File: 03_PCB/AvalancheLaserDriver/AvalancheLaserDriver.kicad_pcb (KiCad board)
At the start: 2 copper layers, 57 x 32 mm, 58 parts, among them IC1 LT8365JMSE, J1 694106106102, J2 SMA, J3 Conn_01x02_Pin, J4 SMA, Q1 PJA3463_R1_00001, Q2 FMMT417TD, SW1 JS202011JAQN

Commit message: feat(pcb): edit component values after assembling first prototype
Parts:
- C9: value 100n;500V -> 22n;500V
- D8: value SD103AWS -> SD103AWS/PMEG3005EJ
- R1: value 100k -> 100k;1%
- R2: value 47k -> 47k;1%
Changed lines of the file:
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@@
 			)
 		)
-		(property "Value" "SD103AWS"
+		(property "Value" "SD103AWS/PMEG3005EJ"
 			(at 0.1 1.9 0)
 			(layer "F.Fab")
@@
 		(property ki_fp_filters "BarrelJack*")
 		(sheetname "/")
-		(sheetfile "LightspeedLaserDriver.kicad_sch")
+		(sheetfile "AvalancheLaserDriver.kicad_sch")
 		(attr smd)
 		(fp_circle
@@
 		(property ki_fp_filters "MountingHole*")
 		(sheetname "/")
-		(sheetfile "LightspeedLaserDriver.kicad_sch")
+		(sheetfile "AvalancheLaserDriver.kicad_sch")
 		(attr exclude_from_pos_files exclude_from_bom)
 		(fp_circle
@@
 		(property ki_fp_filters "LED* LED_SMD:* LED_THT:*")
 		(sheetname "/")
-		(sheetfile "LightspeedLaserDriver.kicad_sch")
+		(sheetfile "AvalancheLaserDriver.kicad_sch")
 		(attr smd)
 		(fp_line
@@
 			)
 		)
-		(property "Value" "100k"
+		(property "Value" "100k;1%"
 			(at 0 1.43 0)
 			(layer "F.Fab")
@@
 		(property ki_fp_filters "R_*")
 		(sheetname "/")
-		(sheetfile "LightspeedLaserDriver.kicad_sch")
+		(sheetfile "AvalancheLaserDriver.kicad_sch")
 		(attr smd)
 		(fp_line
@@
 		(property ki_fp_filters "Connector*:*_1x??_*")
 		(sheetname "/")
-		(sheetfile "LightspeedLaserDriver.kicad_sch")
+		(sheetfile "AvalancheLaserDriver.kicad_sch")
 		(attr smd)
 		(fp_rect
@@
 		(property ki_fp_filters "TO-???* *_Diode_* *SingleDiode* D_*")
 		(sheetname "/")
-		(sheetfile "LightspeedLaserDriver.kicad_sch")
+		(sheetfile "AvalancheLaserDriver.kicad_sch")
 		(attr smd)
 		(fp_line
@@
 		(property ki_fp_filters "MountingHole*")
 		(sheetname "/")
-		(sheetfile "LightspeedLaserDriver.kicad_sch")
+		(sheetfile "AvalancheLaserDriver.kicad_sch")
 		(attr exclude_from_pos_files exclude_from_bom)
 		(fp_circle
@@
 		(property ki_fp_filters "*Fuse*")
 		(sheetname "/")
-		(sheetfile "LightspeedLaserDriver.kicad_sch")
+		(sheetfile "AvalancheLaserDriver.kicad_sch")
 		(attr smd)
 		(fp_line
@@
 		(property ki_fp_filters "MountingHole*")
 		(sheetname "/")
-		(sheetfile "LightspeedLaserDriver.kicad_sch")
+		(sheetfile "AvalancheLaserDriver.kicad_sch")
 		(attr exclude_from_pos_files exclude_from_bom)
 		(fp_circle
@@
 			)
 		)
-		(property "Value" "100n;500V"
+		(property "Value" "22n;500V"
 			(at 0 1.68 90)
 			(layer "F.Fab")
@@
 		(property ki_fp_filters "MountingHole*")
 		(sheetname "/")
-		(sheetfile "LightspeedLaserDriver.kicad_sch")
+		(sheetfile "AvalancheLaserDriver.kicad_sch")
 		(attr exclude_from_pos_files exclude_from_bom)
 		(fp_circle
@@
 		)
 		(sheetname "/")
-		(sheetfile "LightspeedLaserDriver.kicad_sch")
+		(sheetfile "AvalancheLaserDriver.kicad_sch")
 		(attr smd)
 		(fp_line
@@
 			)
 		)
-		(property "Value" "47k"
+		(property "Value" "47k;1%"
 			(at 0 1.43 0)
 			(layer "F.Fab")
@@
 		(property ki_fp_filters "R_*")
 		(sheetname "/")
-		(sheetfile "LightspeedLaserDriver.kicad_sch")
+		(sheetfile "AvalancheLaserDriver.kicad_sch")
 		(attr smd)
 		(fp_line
@@
 		(property ki_fp_filters "*BNC* *SMA* *SMB* *SMC* *Cinch* *LEMO* *UMRF* *MCX* *U.FL*")
 		(sheetname "/")
-		(sheetfile "LightspeedLaserDriver.kicad_sch")
+		(sheetfile "AvalancheLaserDriver.kicad_sch")
 		(attr through_hole)
 		(fp_line
@@
 		(property ki_fp_filters "*BNC* *SMA* *SMB* *SMC* *Cinch* *LEMO* *UMRF* *MCX* *U.FL*")
 		(sheetname "/")
-		(sheetfile "LightspeedLaserDriver.kicad_sch")
+		(sheetfile "AvalancheLaserDriver.kicad_sch")
 		(attr through_hole)
 		(fp_line

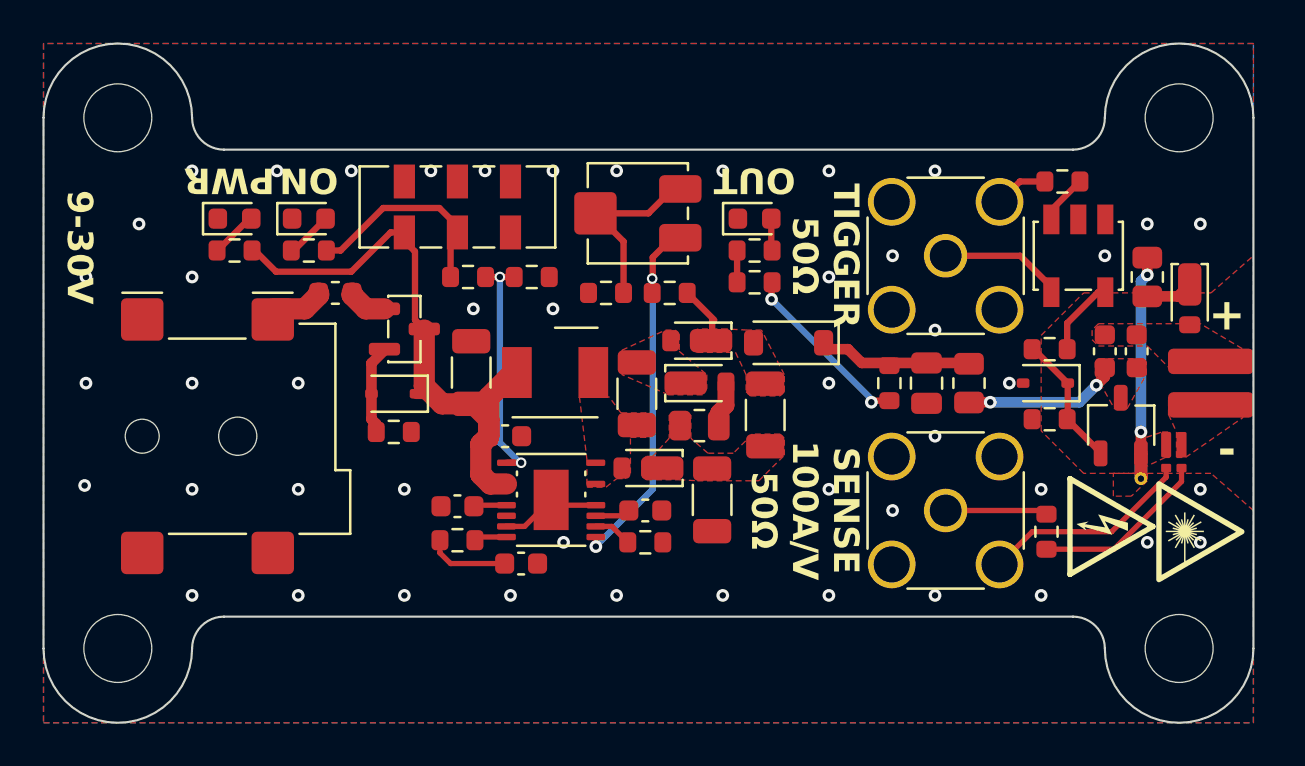
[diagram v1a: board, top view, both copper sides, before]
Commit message: feat(pcb): update laser driver circuit after first iteration
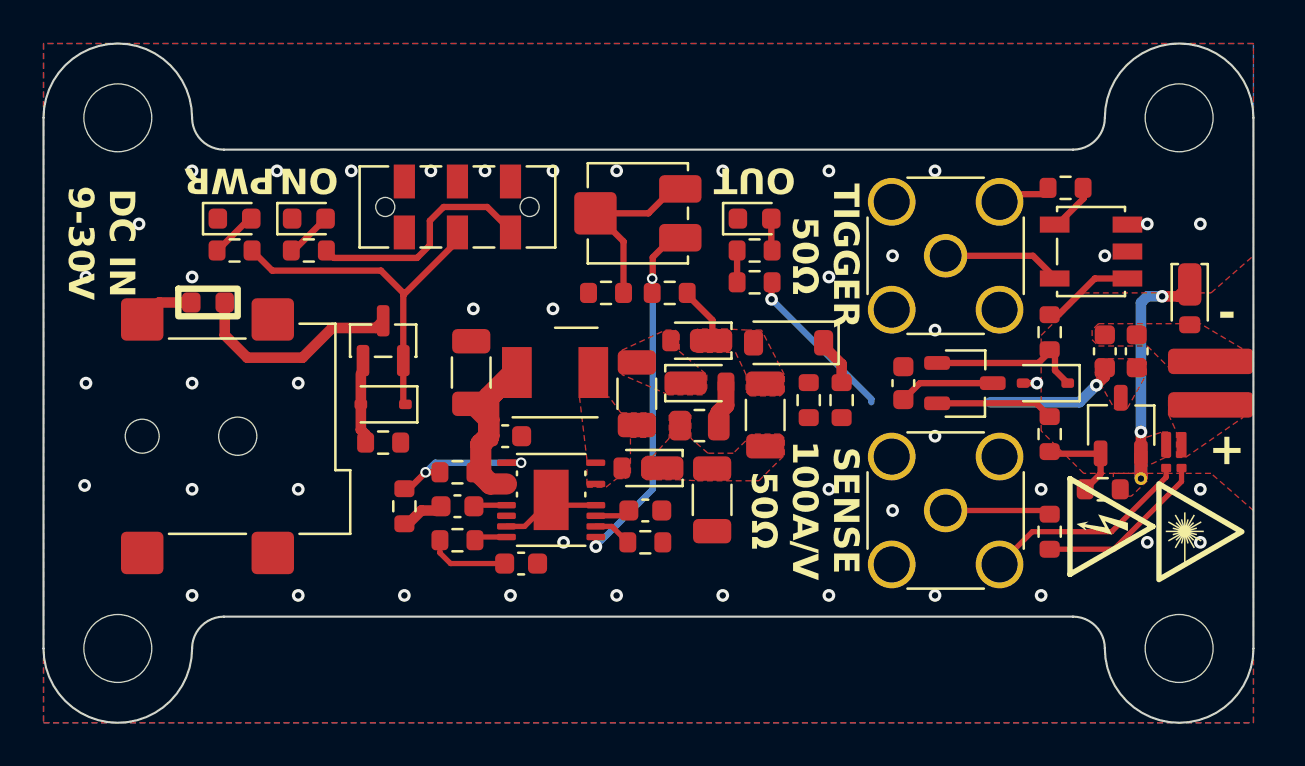
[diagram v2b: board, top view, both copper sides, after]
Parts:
- removed R20: 100k;1%, Resistor_SMD:R_0603_1608Metric
- added Q3: PMBT6429-QR, Package_TO_SOT_SMD:TSOT-23, F.Cu at (146.4, 110.0)
- added R21: 10k;1%, Resistor_SMD:R_0603_1608Metric, F.Cu at (152.9, 115.0)
- C9: value 22n;500V -> 100n;100V; footprint Capacitor_SMD:C_0805_2012Metric -> Capacitor_SMD:C_0603_1608Metric
- D8: value SD103AWS/PMEG3005EJ -> PMEG3005EJ
- R12: value 2k;1% -> 10k;1%; footprint Resistor_SMD:R_0805_2012Metric -> Resistor_SMD:R_0603_1608Metric
- R14: value 2k;1% -> 50;1%; footprint Resistor_SMD:R_0805_2012Metric -> Resistor_SMD:R_0603_1608Metric
- moved R10 12.4 mm to (120.0, 115.8), turned to 90 degrees
- moved R9 9.21 mm to (122.5, 114.2), turned to 0 degrees
- moved R14 8.71 mm to (150.4, 112.4)
- moved R12 6.05 mm to (140.6, 110.8)
- moved F1 6.02 mm to (110.8, 106.2)
- moved R18 3.88 mm to (139.1, 110.8)
- moved Q1 1.14 mm to (119.0, 108.0), turned to 90 degrees
- moved C9 1.09 mm to (143.5, 110.0)
- moved R11 0.80 mm to (150.4, 107.6), turned to -90 degrees
- moved D1 0.71 mm to (119.0, 111.0)
- moved R1 0.71 mm to (119.0, 112.8)
- moved TR1 0.63 mm to (152.3, 103.8), turned to 0 degrees
- moved R13 0.34 mm to (151.2, 100.8)
- moved R15 0.15 mm to (150.4, 117.0)
- turned R8 to 0 degrees
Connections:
- net Net-(F1-Pad1) renamed /Input Protection/VIN
- C9 pad 1: /Driver Stage/HV_DRIVER -> GND
- C9 pad 2: GND -> /Boost Converter/VIN
- D1 pad 1: /Boost Converter/VIN -> Net-(D1-K)
- D8 pad 1: /Driver Stage/TRIG -> Net-(D8-K)
- D9 pad 1: Net-(D9-K) -> /Driver Stage/DRV_GND
- Q1 pad 1: Net-(Q1-D) -> Net-(D1-A)
- Q1 pad 2: Net-(D1-A) -> Net-(D1-K)
- Q1 pad 3: /Boost Converter/VIN -> Net-(Q1-D)
- R11 pad 2: /Driver Stage/TRIG -> Net-(D8-K)
- R14 pad 1: /Driver Stage/DRV_GND -> Net-(Q3-E)
- R14 pad 2: Net-(D9-K) -> /Driver Stage/TRIG
- R2 pad 1: /Boost Converter/VIN -> Net-(D1-K)
- R8 pad 1: Net-(R8-Pad1) -> Net-(D6-A)
- R8 pad 2: Net-(D6-A) -> /Boost Converter/VIN
- R9 pad 2: Net-(R8-Pad1) -> /Boost Converter/VIN
- SW1 pad 1: GND -> /Boost Converter/VIN
- SW1 pad 2: Net-(R8-Pad1) -> Net-(D1-K)
- SW1 pad 3: /Boost Converter/VIN -> unconnected-(SW1-C-Pad3)
- TR1 pad 1: /Driver Stage/TRIG_IN_+ -> Net-(R13-Pad1)
- TR1 pad 2: Net-(R11-Pad1) -> /Driver Stage/TRIG_IN_+
- TR1 pad 3: GND -> Net-(R11-Pad1)
- TR1 pad 4: GND -> unconnected-(TR1-Pad4)
- TR1 pad 5: Net-(R13-Pad1) -> GND
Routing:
- net Net-(D1-K): track 0.00 -> 17.3 mm
- net Net-(R8-Pad1): track 8.88 -> 0.00 mm
- net Net-(Q1-D): track 1.89 -> 10.2 mm
- net Net-(D8-K): track 0.00 -> 7.55 mm
- net Net-(Q3-E): track 0.00 -> 5.70 mm
- net /Driver Stage/HV_DRIVER: track 7.11 -> 2.40 mm
- net /Boost Converter/EN: track 11.2 -> 7.37 mm
- net /Boost Converter/VIN: track 30.0 -> 26.8 mm
- net GND: track 4.48 -> 7.10 mm, vias 47 -> 45
- net Net-(D9-K): track 2.23 -> 0.00 mm
- net /Driver Stage/TRIG: track 6.18 -> 4.30 mm
- net /Driver Stage/DRIVER_CAPS: track 7.31 -> 6.32 mm, vias 2 -> 1
- net Net-(R17-Pad1): track 8.38 -> 7.50 mm, vias 2 -> 1
- net Net-(D1-A): track 4.20 -> 3.33 mm
- net Net-(R11-Pad1): track 3.62 -> 4.32 mm
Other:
- board text added: "DC IN 9-30V"
- board text removed: "9-30V"

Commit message: feat(pcb): Increase operating voltage to 320V
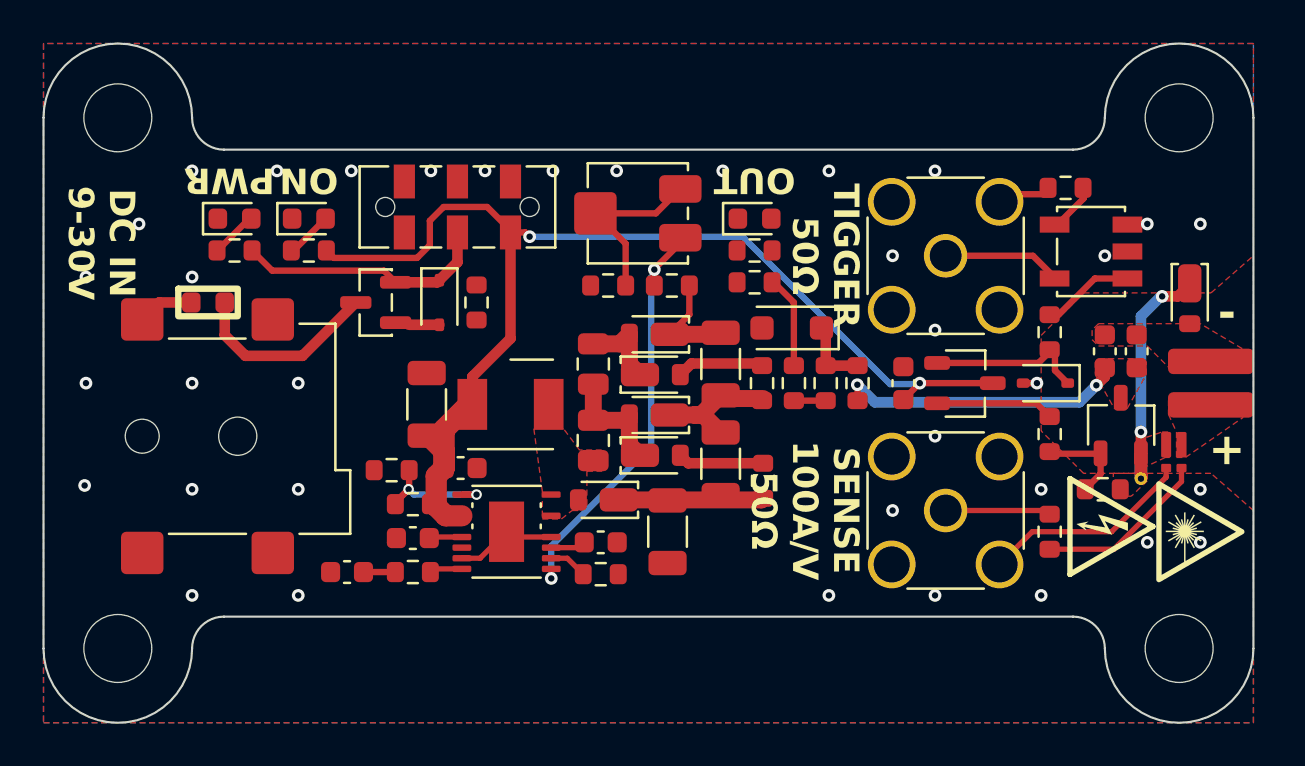
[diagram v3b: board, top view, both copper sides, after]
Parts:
- added C10: 100n;200V, Capacitor_SMD:C_0805_2012Metric, F.Cu at (128.9, 109.1)
- added C13: 220n;200V, Capacitor_SMD:C_1206_3216Metric, F.Cu at (134.9, 109.1)
- added D11: SMD115PBQ-TP, CustomFootprints:D_SOD-323HE, F.Cu at (131.8, 109.6)
- added D12: SMD115PBQ-TP, CustomFootprints:D_SOD-323HE, F.Cu at (131.8, 107.7)
- added R20: 20;1%, Resistor_SMD:R_0603_1608Metric, F.Cu at (136.8, 110.0)
- added R22: 160k;1%, Resistor_SMD:R_0603_1608Metric, F.Cu at (138.3, 110.0)
- C6: footprint Capacitor_SMD:C_1206_3216Metric -> Capacitor_SMD:C_0805_2012Metric
- D7: footprint Diode_SMD:D_SOD-123 -> Diode_SMD:D_SOD-123F
- R5: footprint Resistor_SMD:R_0805_2012Metric -> Resistor_SMD:R_0603_1608Metric
- R7: value 6.2k;1% -> 4.99k;1%
- RV1: value 3314J-1-103G -> 3314J-1-473G
- moved C4 8.21 mm to (117.3, 118.9), turned to 0 degrees
- moved R1 7.93 mm to (123.4, 106.2), turned to 90 degrees
- moved D1 5.48 mm to (121.7, 106.2), turned to -90 degrees
- moved D5 4.03 mm to (131.8, 111.5)
- moved D4 4.00 mm to (131.8, 113.4)
- moved R5 3.97 mm to (136.9, 114.6), turned to -90 degrees
- moved C7 3.11 mm to (134.9, 113.8)
- moved C6 3.01 mm to (128.9, 112.7)
- moved C1 2.58 mm to (121.0, 111.0)
- moved IC1 2.58 mm to (124.8, 117.0)
- moved C2 2.58 mm to (122.7, 114.0)
- moved C3 2.58 mm to (120.4, 117.3)
- moved C5 2.58 mm to (129.2, 117.5)
- moved C8 2.58 mm to (132.4, 117.0)
- moved D3 2.58 mm to (129.4, 115.5)
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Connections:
- C6 pad 2: /Boost Converter/BOOST_NODE2 -> /Boost Converter/BOOST_NODE3
- C7 pad 1: /Boost Converter/BOOST_NODE3 -> /Boost Converter/BOOST_NODE2
- C7 pad 2: /Boost Converter/HV_OUT -> Net-(D5-K)
- C8 pad 2: /Boost Converter/BOOST_NODE3 -> /Boost Converter/BOOST_NODE2
- D3 pad 1: /Boost Converter/BOOST_NODE3 -> /Boost Converter/BOOST_NODE2
- D4 pad 1: /Boost Converter/BOOST_NODE2 -> /Boost Converter/BOOST_NODE3
- D5 pad 1: /Boost Converter/HV_OUT -> Net-(D5-K)
- D5 pad 2: /Boost Converter/BOOST_NODE2 -> /Boost Converter/BOOST_NODE3
- R18 pad 2: Net-(R17-Pad1) -> Net-(R18-Pad2)
- R5 pad 2: /Boost Converter/BOOST_NODE3 -> /Boost Converter/BOOST_NODE2
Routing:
- net /Boost Converter/VIN: track 26.8 -> 58.0 mm, vias 0 -> 2
- net /Driver Stage/DRIVER_CAPS: track 6.32 -> 13.7 mm, vias 1 -> 2
- net /Boost Converter/BOOST_NODE2: track 0.00 -> 6.83 mm
- net Net-(D5-K): track 0.00 -> 6.44 mm
- net /Boost Converter/BOOST_NODE3: track 0.00 -> 5.61 mm
- net Net-(D1-K): track 17.3 -> 12.1 mm
- net Net-(D11-A): track 0.00 -> 4.12 mm
- net /Boost Converter/BOOST_NODE4: track 0.00 -> 3.99 mm
- net Net-(R17-Pad1): track 7.50 -> 4.46 mm, vias 1 -> 0
- net Net-(C4-Pad2): track 3.86 -> 1.50 mm
- net /Boost Converter/HV_OUT: track 2.77 -> 5.11 mm
- net /Boost Converter/FBX: track 17.2 -> 19.4 mm
- net Net-(D4-A): track 2.14 -> 4.06 mm
- net Net-(D1-A): track 3.33 -> 1.44 mm
- net GND: track 7.10 -> 5.35 mm, vias 45 -> 36
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- removed copper zone on F.Cu, net /Boost Converter/BOOST_NODE2
- removed copper zone on F.Cu, net /Boost Converter/BOOST_NODE3
- removed copper zone on F.Cu, net /Boost Converter/HV_OUT

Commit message: feat(pcb): finalize layout of PCB V0.2
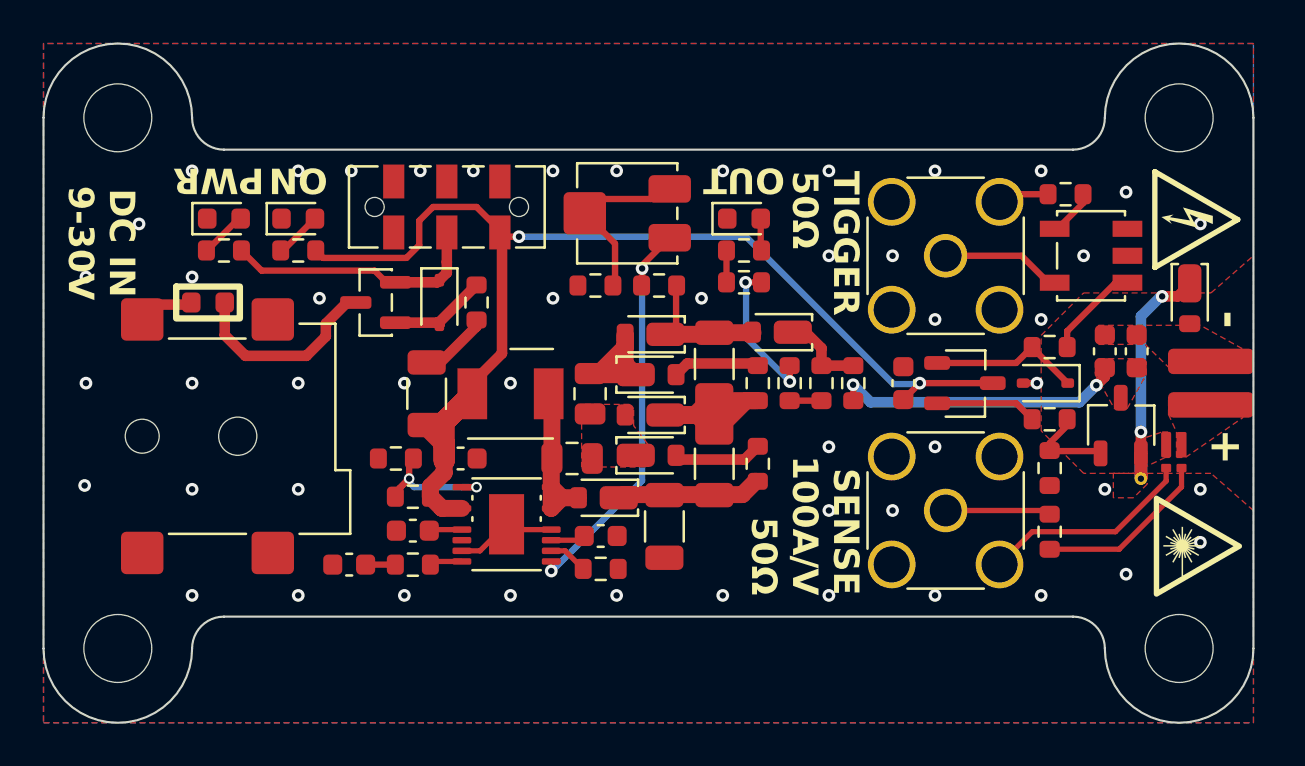
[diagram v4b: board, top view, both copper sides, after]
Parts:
- D7: value US1MHM3 -> SRL1G; footprint Diode_SMD:D_SOD-123F -> CustomFootprints:D_SOD-323HE
- moved R21 2.69 mm to (150.4, 114.0), turned to -90 degrees
- moved C10 1.41 mm to (128.8, 110.5)
- moved C6 1.31 mm to (127.9, 113.5), turned to 0 degrees
- moved R5 0.84 mm to (136.7, 113.8)
- moved R11 0.70 mm to (150.4, 108.3), turned to 180 degrees
- moved R14 0.70 mm to (150.4, 111.7), turned to 0 degrees
- moved D7 0.68 mm to (137.6, 107.6)
- moved R6 0.60 mm to (132.0, 105.4)
- moved R7 0.60 mm to (129.0, 105.4)
- moved R10 0.59 mm to (119.6, 113.5)
- moved C1 0.50 mm to (121.0, 110.5)
- moved D10 0.50 mm to (136.0, 102.2)
- moved D2 0.50 mm to (111.5, 102.2)
- moved D6 0.50 mm to (115.0, 102.2)
- moved L1 0.50 mm to (125.0, 110.5)
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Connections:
- C11 pad 2: /Driver Stage/D+ -> /Driver Stage/D-
- C12 pad 2: /Driver Stage/D+ -> /Driver Stage/D-
- D9 pad 2: /Driver Stage/D+ -> /Driver Stage/D-
- R19 pad 1: /Driver Stage/D- -> /Driver Stage/D+
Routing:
- net Net-(D5-K): track 6.44 -> 15.5 mm
- net /Boost Converter/BOOST_NODE1: track 0.00 -> 7.52 mm
- net /Boost Converter/BOOST_NODE3: track 5.61 -> 0.00 mm
- net GND: track 5.35 -> 8.76 mm, vias 36 -> 50
- net Net-(D1-A): track 1.44 -> 4.70 mm
- net /Boost Converter/BOOST_NODE4: track 3.99 -> 6.97 mm
- net Net-(R17-Pad1): track 4.46 -> 7.04 mm, vias 0 -> 2
- net /Boost Converter/HV_OUT: track 5.11 -> 6.79 mm
- net Net-(D10-A): track 0.00 -> 1.52 mm
- net Net-(R16-Pad1): track 0.00 -> 1.50 mm
- net Net-(Q3-E): track 5.70 -> 4.79 mm
- net /Boost Converter/VIN: track 58.0 -> 57.2 mm
- net /Driver Stage/HV_DRIVER: track 3.36 -> 3.99 mm
- added copper zone on F.Cu, net /Boost Converter/BOOST_NODE3
- removed copper zone on F.Cu, net /Boost Converter/BOOST_NODE1
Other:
- board text added: "Fixed Pulsewidth Avalanche Laser Driver Output adjustable between 170-320V (c) Hannes Duske 2026 V0.2"
- board text removed: "Fixed Pulsewidth Avalanche Laser Driver Output adjustable between 100-260V (c) Hannes Duske 2026 V0.1"

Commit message: feat(pcb): laser driver V0.2 as ordered on 08.04.2026
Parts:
- R12: value 10k;1% -> 47k;1%
- moved D8 0.20 mm to (150.4, 110.0), turned to 0 degrees
- moved D7 0.10 mm to (137.6, 107.7)
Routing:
- net GND: track 8.76 -> 15.8 mm
- net /Boost Converter/VIN: track 57.2 -> 58.4 mm
